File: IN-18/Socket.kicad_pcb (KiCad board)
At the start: 2 copper layers, 220 x 65 mm, 19 parts, among them J1 CONNECTOR, J2 CONNECTOR, J3 CONNECTOR, J4 CONNECTOR, J5 CONNECTOR, J6 CONNECTOR, T1 TUBE, T2 TUBE, T3 TUBE, T4 TUBE, T5 TUBE, T6 TUBE

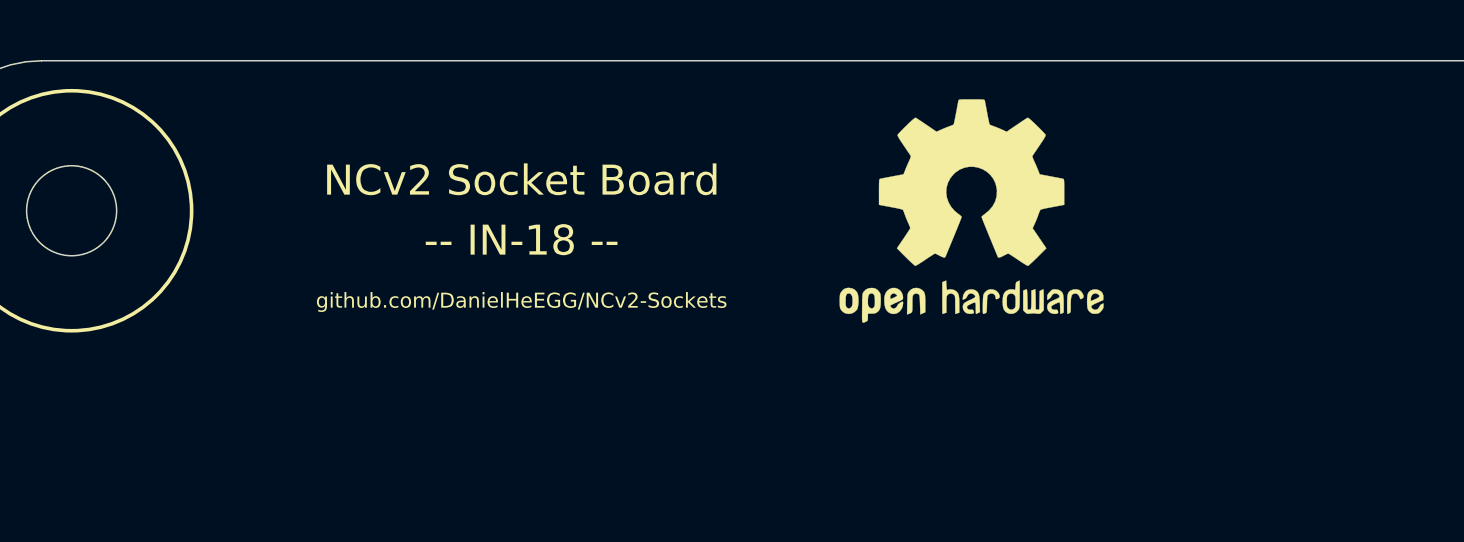
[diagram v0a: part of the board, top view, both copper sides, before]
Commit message: Increase silkscreen text size
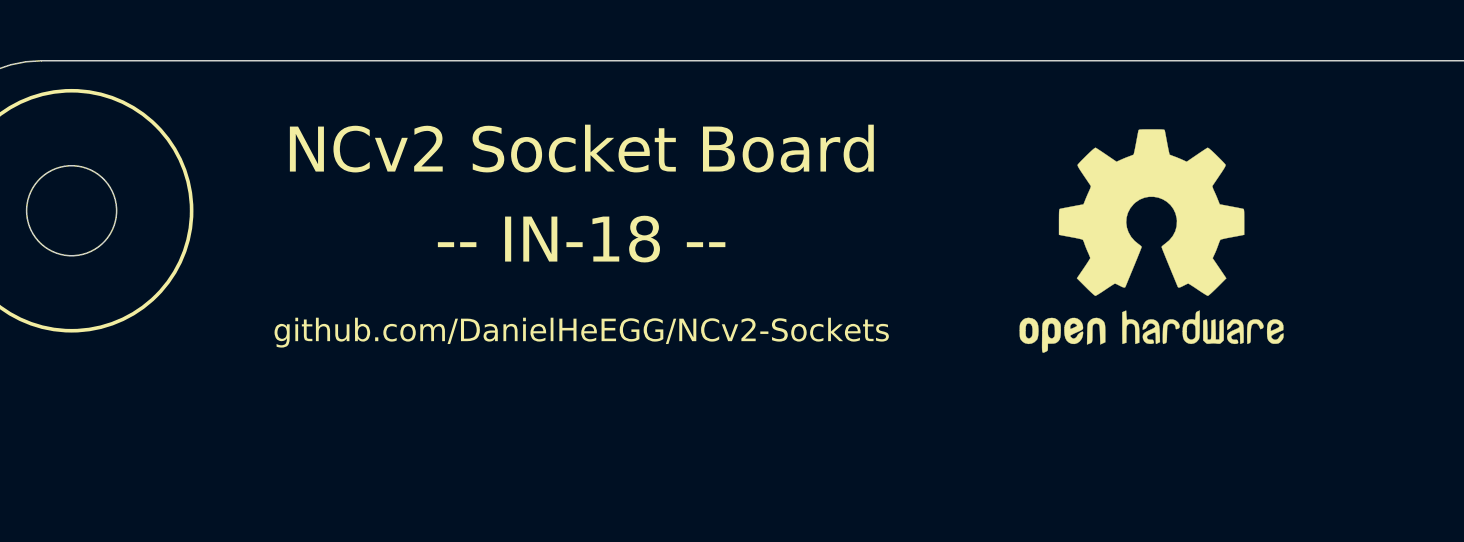
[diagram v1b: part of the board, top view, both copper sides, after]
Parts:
- moved REF** 6.08 mm to (86.0, 66.0)
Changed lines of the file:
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@@
   )
   (module Symbol:OSHW-Logo2_9.8x8mm_SilkScreen (layer F.Cu)
-    (at 80 65)
+    (at 86 66)
     (descr "Open Source Hardware Symbol")
     (tags "Logo Symbol OSHW")
@@
     (effects (font (size 0.5 0.5) (thickness 0.1)))
   )
-  (gr_text "-- IN-18 --" (at 65 66) (layer F.SilkS)
-    (effects (font (size 1 1) (thickness 0.15)))
-  )
-  (gr_text github.com/DanielHeEGG/NCv2-Sockets (at 65 68) (layer F.SilkS)
-    (effects (font (size 0.5 0.5) (thickness 0.1)))
-  )
-  (gr_text "NCv2 Socket Board" (at 65 64) (layer F.SilkS)
-    (effects (font (size 1 1) (thickness 0.15)))
+  (gr_text "-- IN-18 --" (at 67 66) (layer F.SilkS)
+    (effects (font (size 1.5 1.5) (thickness 0.2)))
+  )
+  (gr_text github.com/DanielHeEGG/NCv2-Sockets (at 67 69) (layer F.SilkS)
+    (effects (font (size 0.75 0.75) (thickness 0.1)))
+  )
+  (gr_text "NCv2 Socket Board" (at 67 63) (layer F.SilkS)
+    (effects (font (size 1.5 1.5) (thickness 0.2)))
   )
   (gr_line (start 261 60) (end 49 60) (layer Edge.Cuts) (width 0.05))
@@
   (segment (start 149.348646 81.848646) (end 142.980735 81.848646) (width 0.25) (layer B.Cu) (net 44))
   (segment (start 142.980735 81.848646) (end 141.480736 83.348645) (width 0.25) (layer B.Cu) (net 44))
-  (segment (start 104.75 100.207412) (end 104.732239 100.189651) (width 0.25) (layer B.Cu) (net 51))
   (segment (start 106.5 88.489229) (end 106.5 94.066166) (width 0.25) (layer B.Cu) (net 45))
   (segment (start 103.480736 85.469965) (end 106.5 88.489229) (width 0.25) (layer B.Cu) (net 45))
@@
   (segment (start 107.792386 111.507614) (end 107.792386 97.904531) (width 0.25) (layer B.Cu) (net 50))
   (segment (start 99.3 120) (end 107.792386 111.507614) (width 0.25) (layer B.Cu) (net 50))
+  (segment (start 104.75 100.207412) (end 104.732239 100.189651) (width 0.25) (layer B.Cu) (net 51))
   (segment (start 96.76 120) (end 104.75 112.01) (width 0.25) (layer B.Cu) (net 51))
   (segment (start 104.75 100.207412) (end 104.732239 100.189651) (width 0.25) (layer B.Cu) (net 51))

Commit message: Migrate to KiCAD 6
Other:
- net class Default removed
